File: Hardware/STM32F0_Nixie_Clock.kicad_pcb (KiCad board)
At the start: 2 copper layers, 100 x 50 mm, 64 parts, among them P101 USB-C Socket, Q101 IRF740S, SW101 Reset, U101 STM32F042F6P6, U102 AMS1117-3.3, U103 DS3231M, U104 MAX1771, U105 HV5222PLCC, U106 HV5222PLCC

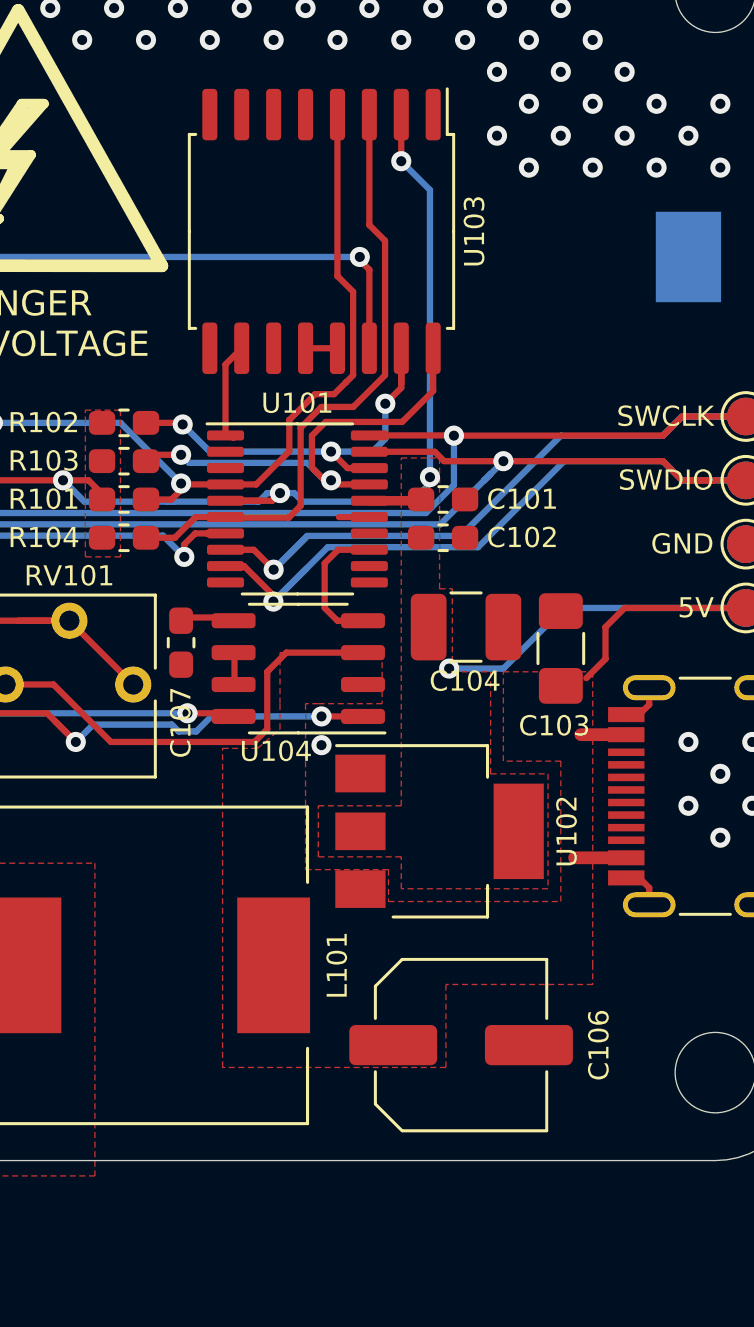
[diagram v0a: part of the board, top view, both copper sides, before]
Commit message: Add decoupling decapacitor to RTC
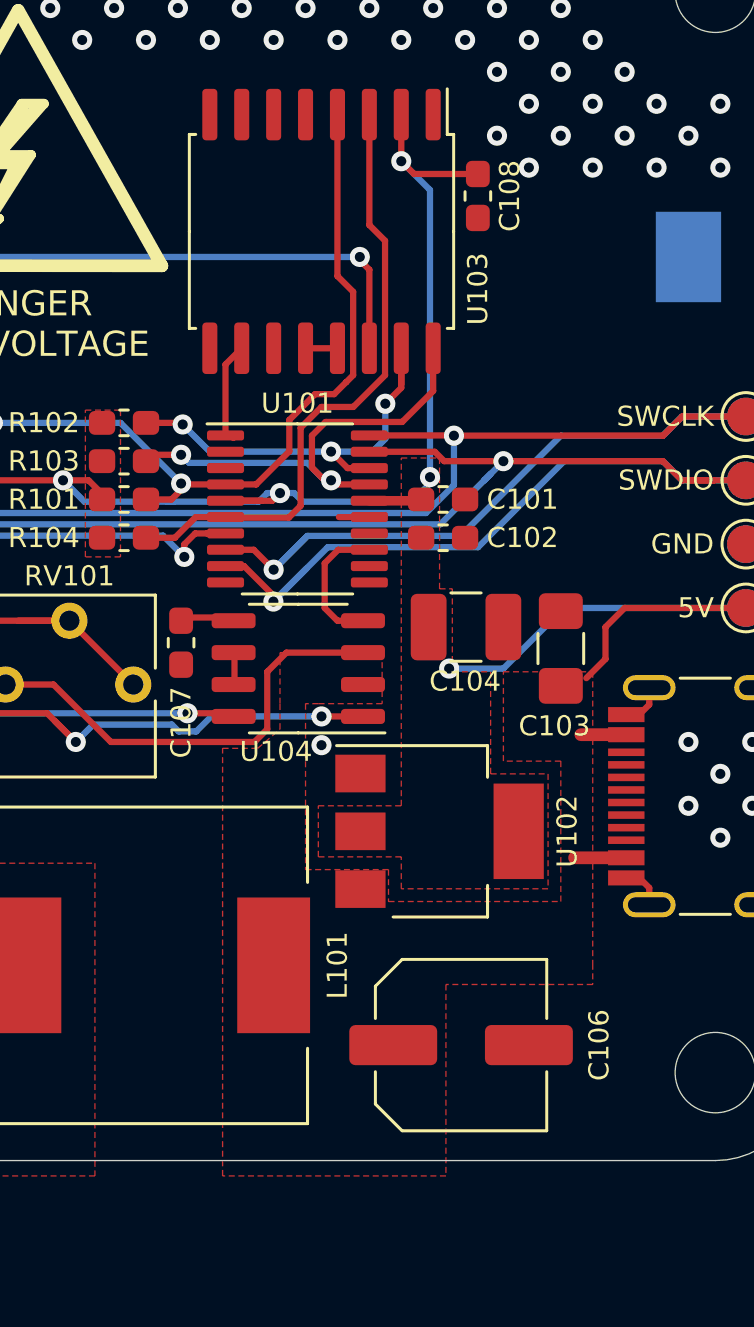
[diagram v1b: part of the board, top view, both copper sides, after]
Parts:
- added C108: 100n, Capacitor_SMD:C_0603_1608Metric_Pad1.05x0.95mm_HandSolder, F.Cu at (193.5, 95.1)
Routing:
- net +3V3: track 126.4 -> 129.7 mm

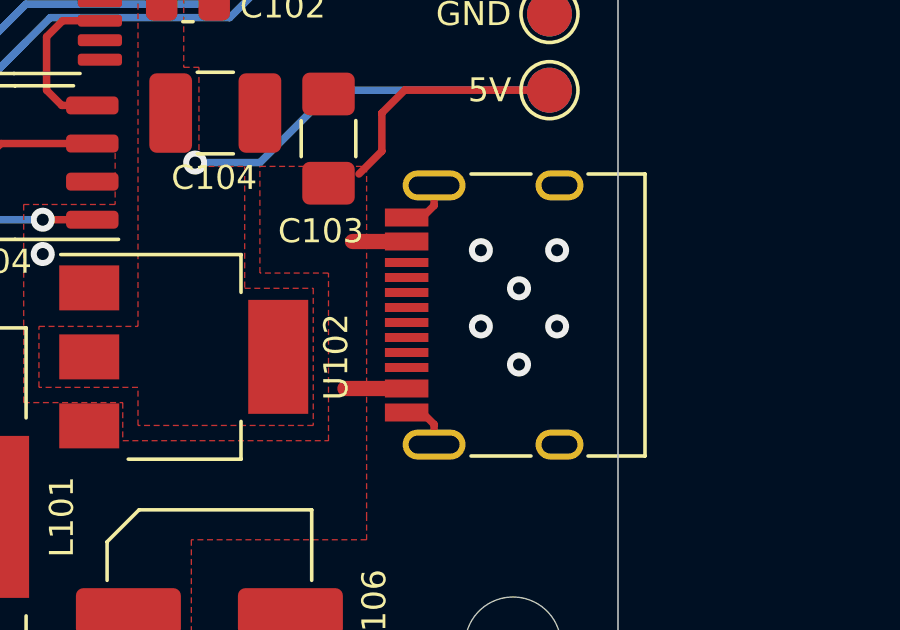
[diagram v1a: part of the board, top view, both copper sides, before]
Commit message: Replace USB-C receptacle symbol
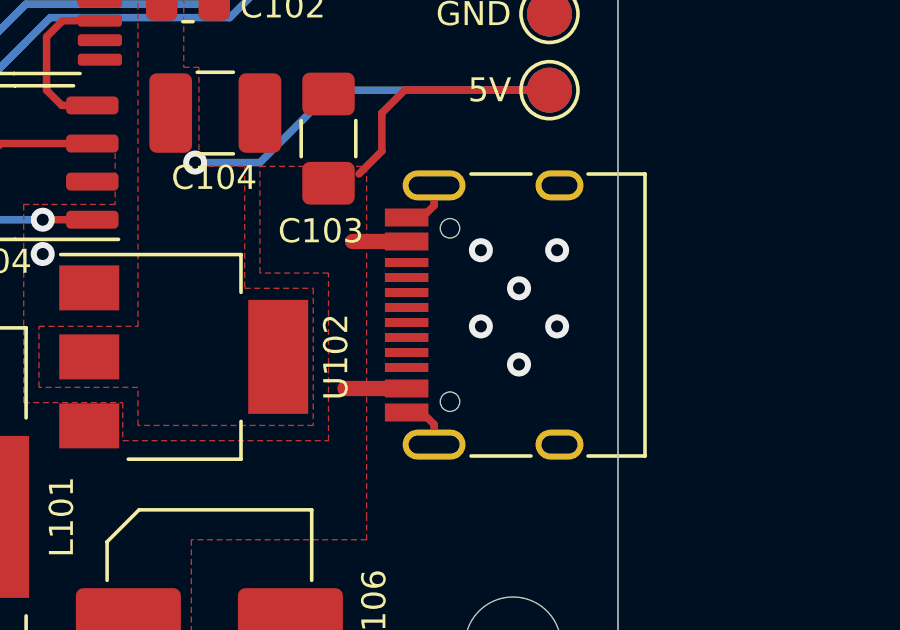
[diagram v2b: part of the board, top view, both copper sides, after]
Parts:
- removed P101: USB-C Socket, Connector_USB:USB_C_Receptacle_HRO_TYPE-C-31-M-12
- added J101: USB-C Receptacle, Connector_USB:USB_C_Receptacle_HRO_TYPE-C-31-M-12, F.Cu at (203.5, 119.0)
